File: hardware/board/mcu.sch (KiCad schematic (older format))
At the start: 24 parts, among them J3 USB_B, J4 Tag-Connect_SWD_TC2030, SW2 Reset, U5 ATSAMD51J20A-M, U6 AD5685R?RUZ, Y1 32.768 kHz

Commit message: Re-do the motherboard
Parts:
- removed C15, C16: 0.1uF, Capacitor_SMD:C_0603_1608Metric_Pad1.08x0.95mm_HandSolder, symbol Device:C_Small
- removed C17: 1uF, Capacitor_SMD:C_0603_1608Metric_Pad1.08x0.95mm_HandSolder, symbol Device:C_Small
- removed FB4: 300mA, Inductor_SMD:L_0603_1608Metric_Pad1.05x0.95mm_HandSolder, symbol Device:Ferrite_Bead_Small
- removed J3: USB_B, Connector_USB:USB_B_OST_USB-B1HSxx_Horizontal, symbol testkit-rescue:USB_B-Connector
- removed J4: Tag-Connect_SWD_TC2030, winterbloom:Tag_Connect_TC2030NL, symbol winterbloom:Tag-Connect_SWD_TC2030
- removed R59, R60: 1k, Resistor_SMD:R_0603_1608Metric_Pad0.98x0.95mm_HandSolder, symbol Device:R_US
- removed U6: AD5685R?RUZ, Package_SO:TSSOP-16_4.4x5mm_P0.65mm, symbol winterbloom:AD5685R?RUZ
- added C5: 4.7nF, Capacitor_SMD:C_0603_1608Metric_Pad1.08x0.95mm_HandSolder, symbol Device:C_Small
- added D7: ACT, winterbloom:LED_0805_Kingbright_APT2012, symbol Device:LED_ALT
- added D8: VBUS, winterbloom:LED_0805_Kingbright_APT2012, symbol Device:LED_ALT
- added J2: SWD, Connector_PinHeader_1.27mm:PinHeader_2x05_P1.27mm_Vertical, symbol Connector:Conn_ARM_JTAG_SWD_10
- added J3: USB_B_Receptacle, Connector_USB:USB_B_OST_USB-B1HSxx_Horizontal, symbol winterbloom:USB_B_Receptacle
- added R35, R6: 1k, Resistor_SMD:R_0603_1608Metric_Pad0.98x0.95mm_HandSolder, symbol Device:R_US
- added R5: 1M, Resistor_SMD:R_0805_2012Metric_Pad1.20x1.40mm_HandSolder, symbol Device:R_US
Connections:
- net A11 is gone; now on net A3: U5.11 (PB08)
- net A12 is gone; now on net A2: U5.12 (PB09)
- net A7 is gone; now on net A1: U5.5 (PB04)
- net A8 is gone; now on net A4: U5.6 (PB05)
- net VDDANA is gone; now on net ADC0.AIN1+ANAREF.VREF0: C6.1, FB3.1, U5.8 (VDDANA)
- net +3V3: now also J2.1 (VTref)
- net A1: no longer U5.61 (PB00)
- net A2: no longer U5.62 (PB01)
- net A3: no longer U5.63 (PB02)
- net A4: no longer U5.64 (PB03)
- net D+: now also J3.3 (D+)
- net D-: now also J3.2 (D-)
- net GND: now also C5.2, D7.1 (K), D8.1 (K), J2.3 (GND), J2.5 (GND), J2.9 (GNDDetect), J3.4 (GND), R5.2
- net RESET: now also J2.10 (~RESET~)
- net SWCLK: now also J2.4 (SWDCLK/TCK)
- net SWDIO: now also J2.2 (SWDIO/TMS)
- net A10 renamed PB07
- net A13 renamed PA04
- net A14 renamed PA05+DAC1
- net A15 renamed PA06
- net A16 renamed PA07
- net A17 renamed PA09
- net A18 renamed PA08
- net A19 renamed PA11
- net A20 renamed PA10
- net A5 renamed PA02+DAC0
- net A6 renamed ADC0.AIN1+ANAREF.VREF0
- net A9 renamed PB06
- net DB0 renamed PA12
- net DB1 renamed PB10
- net DB2 renamed PB11
- net DR1 renamed PA21
- net DR2 renamed PA20
- net DR3 renamed PB17
- net DR4 renamed PB16
- net I2C_SCL renamed PB31
- net I2C_SDA renamed PB30
- net PB30: now also R6.1
- net SPI_SCLK renamed SPI_SCK
- new net: D8.2 (A), R35.2
- new net: D7.2 (A), R6.2
- new net: C5.1, J3.5 (Shield), R5.1
- new net PB00: U5.61 (PB00)
- new net PB01: U5.62 (PB01)
- new net PB02: U5.63 (PB02)
- new net PB03: U5.64 (PB03)
- new net VBUS: J3.1 (VBUS), R35.1
- no-connect marks 6 -> 5
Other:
- note added: "Required for DAC, see Errata CHIP003-161"
- note added: "TODO: Dotstar ext header"
- note removed: "5.0, 5.1 used by I2C"
- note removed: "Check datasheet for proper shield connection"
- moved on the sheet: C10, C11, C12, C13, C14, C6, C7, C8, C9, D3, FB3, Y1

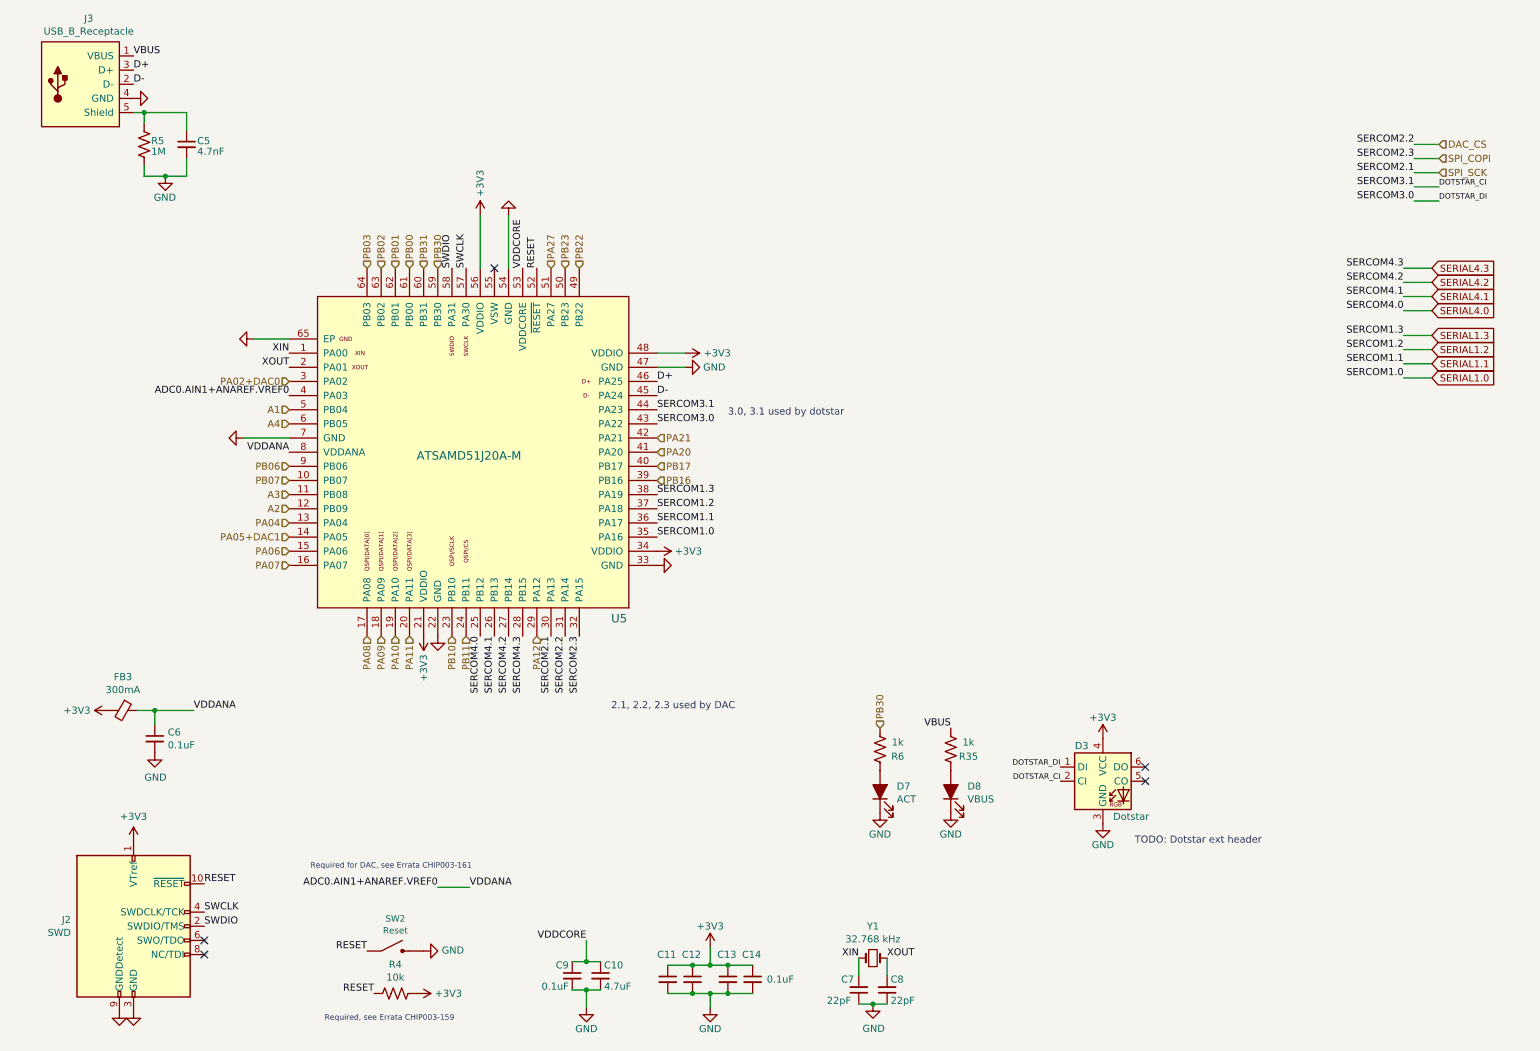
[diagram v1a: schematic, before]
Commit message: Fix issues found in hardware v1
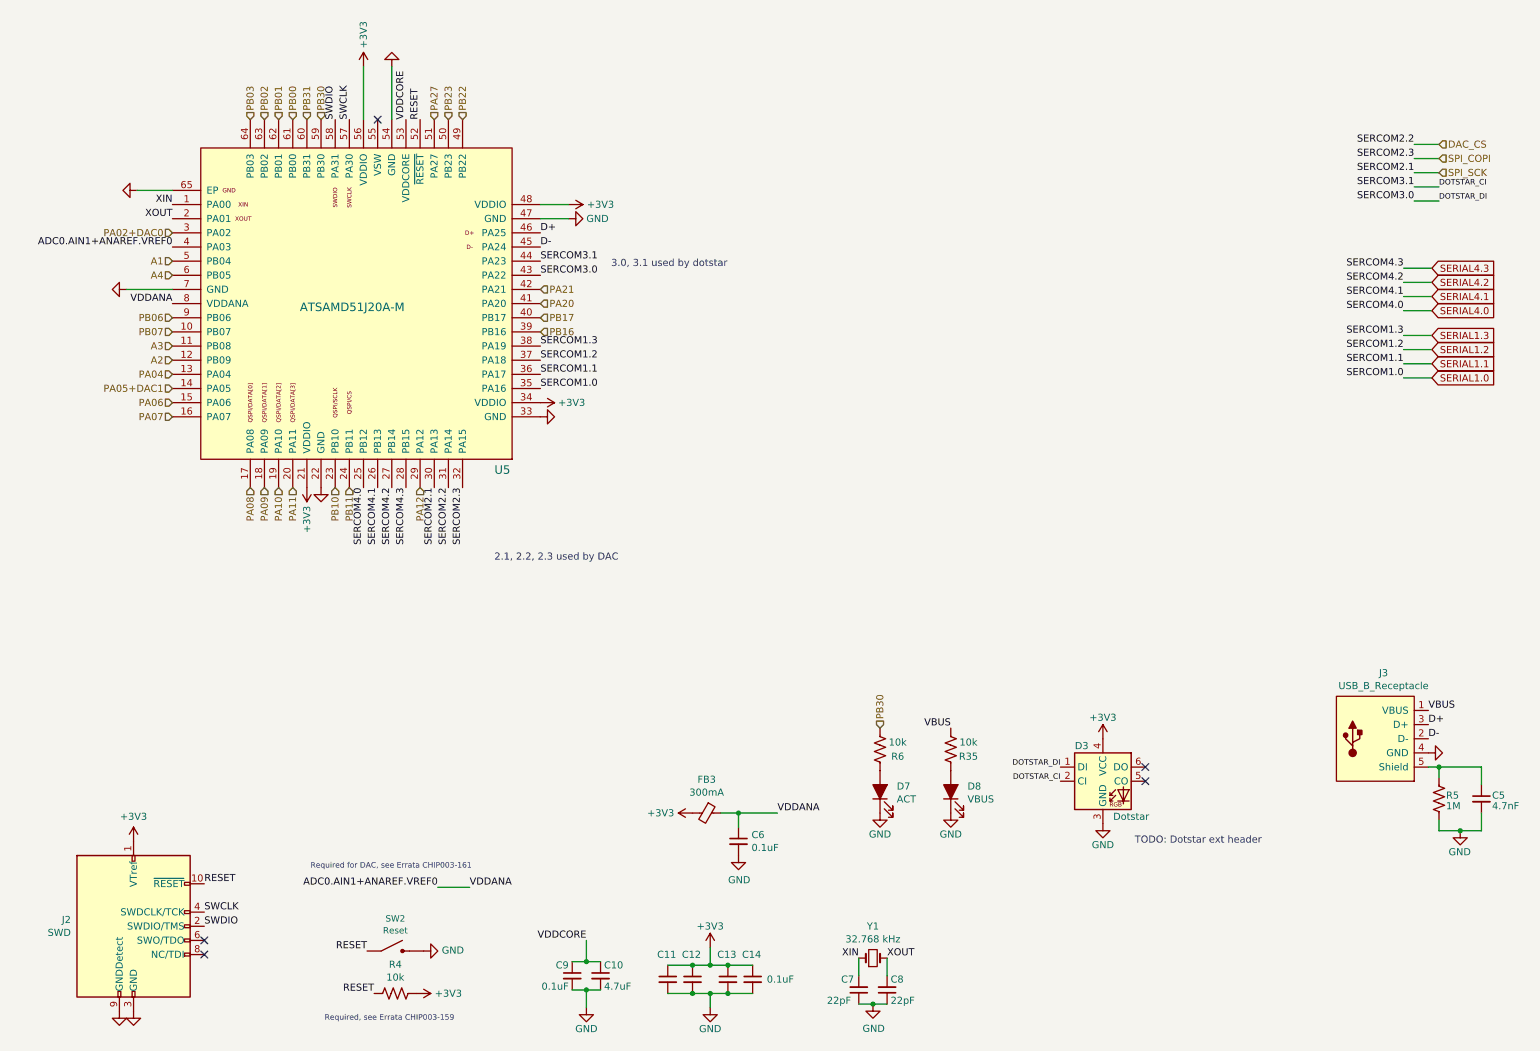
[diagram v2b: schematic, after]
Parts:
- R35, R6: value 1k -> 10k
- U5: footprint Package_DFN_QFN:QFN-64-1EP_9x9mm_P0.5mm_EP3.8x3.8mm -> winterbloom:QFN+QFP-64-SAMD51
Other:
- moved on the sheet: C5, C6, FB3, J3, R5, U5
